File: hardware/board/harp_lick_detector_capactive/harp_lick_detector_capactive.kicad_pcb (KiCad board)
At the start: 4 copper layers, 80 x 50 mm, 170 parts, among them J2 Conn_01x03_Male, J3 Conn_Triaxial, J4 AudioJack3, J5 USB_C_Receptacle_USB2.0, J6 Barrel_Jack_Switch, J7 Conn_Coaxial, SW2 SW_DIP_x02, U1 74LVCH2T45DC, U11 LM27762, U12 LT3030, U13 ADS7049, U14 TS5A9411DCKR, U15 LTC6081xMS8, U16 AD8615, U17 AD8615, U18 TS5A9411DCKR, U2 TPD2EUSB30, U3 ADUM4160, U4 RP2040, U5 W25Q16JVUXIQ, U6 TS5A9411DCKR, U7 LTC6268xS8-10, U8 REF2025, U9 TS5A9411DCKR, X1 ECS-TXO-2016

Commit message: draft v0.8 pcb layout
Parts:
- removed C66: 100nF, Capacitor_SMD:C_0402_1005Metric
- removed U15: LTC6081xMS8, Package_SO:MSOP-8_3x3mm_P0.65mm
- removed U16: AD8615, Package_TO_SOT_SMD:TSOT-23-5
- added C68: 160pF, Capacitor_SMD:C_0402_1005Metric, F.Cu at (134.7, 87.2)
- added C69: 100nF, Capacitor_SMD:C_0402_1005Metric, F.Cu at (140.0, 99.9)
- added C70: 100nF, Capacitor_SMD:C_0402_1005Metric, F.Cu at (138.2, 95.2)
- added C71: 100nF, Capacitor_SMD:C_0402_1005Metric, F.Cu at (132.8, 82.0)
- added C72: 160pF, Capacitor_SMD:C_0402_1005Metric, F.Cu at (133.7, 87.2)
- added C73: 130pF, Capacitor_SMD:C_0402_1005Metric, F.Cu at (134.7, 98.8)
- added C74: 130pF, Capacitor_SMD:C_0402_1005Metric, F.Cu at (133.7, 98.8)
- added R60: 4K7, Resistor_SMD:R_0402_1005Metric, F.Cu at (145.0, 94.5)
- added R61: 4K7, Resistor_SMD:R_0402_1005Metric, F.Cu at (145.0, 95.5)
- added R62: 1K00, Resistor_SMD:R_0402_1005Metric, F.Cu at (141.0, 108.2)
- added R63: 1K00, Resistor_SMD:R_0402_1005Metric, F.Cu at (138.7, 106.5)
- added R64: 200K, Resistor_SMD:R_0402_1005Metric, F.Cu at (132.6, 85.9)
- added R65: 1K00, Resistor_SMD:R_0402_1005Metric, F.Cu at (136.4, 86.8)
- added R66: 100K, Resistor_SMD:R_0402_1005Metric, F.Cu at (134.2, 88.6)
- added R67: 9K76, Resistor_SMD:R_0402_1005Metric, F.Cu at (135.7, 88.2)
- added R68: 147, Resistor_SMD:R_0402_1005Metric, F.Cu at (135.8, 90.1)
- added R69: 249K, Resistor_SMD:R_0402_1005Metric, F.Cu at (132.6, 100.1)
- added R70: 976, Resistor_SMD:R_0402_1005Metric, F.Cu at (136.2, 99.4)
- added R71: 97K6, Resistor_SMD:R_0402_1005Metric, F.Cu at (134.2, 97.4)
- added R72: 8K66, Resistor_SMD:R_0402_1005Metric, F.Cu at (135.7, 97.9)
- added R73: 140, Resistor_SMD:R_0402_1005Metric, F.Cu at (135.8, 96.0)
- added U10: AD8652, Package_SO:MSOP-8_3x3mm_P0.65mm, F.Cu at (141.0, 104.5)
- R51, R53: value 100K -> 1K00
- U14, U18: value TS5A9411DCKR -> MAX4564EKA; footprint Package_TO_SOT_SMD:SOT-363_SC-70-6 -> Package_TO_SOT_SMD:SOT-23-8
- U6: value TS5A9411DCKR -> ADA4891-4; footprint Package_TO_SOT_SMD:SOT-363_SC-70-6 -> Package_SO:TSSOP-14_4.4x5mm_P0.65mm
- moved R52 14.7 mm to (141.0, 109.2), turned to 180 degrees
- moved U9 10.6 mm to (144.4, 104.5), turned to 180 degrees
- moved R49 10.5 mm to (138.3, 105.0), turned to 0 degrees
- moved C64 9.95 mm to (142.8, 109.0), turned to 90 degrees
- moved R51 9.79 mm to (138.3, 104.0), turned to 180 degrees
- moved C25 9.74 mm to (132.6, 88.2), turned to 90 degrees
- moved U6 9.12 mm to (132.6, 93.0)
- moved C60 8.57 mm to (145.4, 102.0), turned to 0 degrees
- moved C24 6.74 mm to (132.6, 97.8)
- moved R53 5.65 mm to (141.7, 99.8), turned to 0 degrees
- moved R46 5.17 mm to (129.3, 90.1), turned to 90 degrees
- moved R56 5.14 mm to (128.0, 82.4)
- moved R24 4.54 mm to (127.8, 98.2), turned to 0 degrees
- moved R27 3.83 mm to (129.4, 88.2), turned to 90 degrees
- moved R19 3.69 mm to (127.9, 86.8), turned to 0 degrees
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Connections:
- C1 pad 2: +3V3 -> +3.3V
- C10 pad 1: +3V3 -> +3.3V
- C11 pad 1: +3V3 -> +3.3V
- C12 pad 2: +3V3 -> +3.3V
- C13 pad 2: +3V3 -> +3.3V
- C14 pad 2: +3V3 -> +3.3V
- C15 pad 2: +3V3 -> +3.3V
- C16 pad 2: +3V3 -> +3.3V
- C17 pad 2: +3V3 -> +3.3V
- C18 pad 2: +3V3 -> +3.3V
- C19 pad 2: +3V3 -> +3.3V
- C29 pad 1: GND -> +2V5
- C29 pad 2: +3V3 -> GND
- C3 pad 2: +3V3 -> +3.3V
- C31 pad 2: Net-(U15B--) -> Net-(U6D--)
- C34 pad 2: Net-(U15A--) -> Net-(U6A--)
- C4 pad 2: +3V3 -> +3.3V
- C47 pad 1: +3V3 -> +3.3V
- C48 pad 1: +3V3 -> +3.3V
- C5 pad 2: +3V3 -> +3.3V
- C51 pad 2: +3V3 -> +3.3V
- C53 pad 1: +3V3 -> +3.3V
- C54 pad 2: +3V3 -> +3.3V
- C60 pad 2: +3V3 -> +3.3V
- C63 pad 2: +3V3 -> +2V5
- C64 pad 2: +3V3 -> +2V5
- C65 pad 2: +2V5 -> VREF_1V25
- C8 pad 1: +3V3 -> +3.3V
- D4 pad 2: +3V3 -> +3.3V
- J4 pad R: +3V3 -> +3.3V
- R20 pad 1: Net-(U15B--) -> Net-(U6D--)
- R21 pad 2: Net-(U16-+) -> Net-(U10A-+)
- R22 pad 1: Net-(U16--) -> Net-(U10A--)
- R23 pad 1: Net-(U7--) -> Net-(C33-Pad1)
- R23 pad 2: Net-(C33-Pad1) -> Net-(U7--)
- R26 pad 1: Net-(U15A--) -> Net-(U6A--)
- R27 pad 1: Net-(U15B-+) -> Net-(U6D-+)
- R39 pad 1: +3V3 -> +3.3V
- R43 pad 2: Net-(R22-Pad2) -> Net-(R43-Pad2)
- R46 pad 2: Net-(U15B-+) -> Net-(U6D-+)
- R47 pad 2: Net-(U15A-+) -> Net-(U6A-+)
- R48 pad 1: Net-(U15A-+) -> Net-(U6A-+)
- R49 pad 2: Net-(R49-Pad2) -> Net-(U10B-+)
- R51 pad 1: Net-(R51-Pad1) -> Net-(U10A-+)
- R51 pad 2: Net-(R49-Pad2) -> Net-(R49-Pad1)
- R52 pad 1: Net-(R52-Pad1) -> GND
- R52 pad 2: GND -> Net-(U10B--)
- R53 pad 1: Net-(R53-Pad1) -> Net-(U10A--)
- R57 pad 2: +3V3 -> +3.3V
- R58 pad 2: +3V3 -> +3.3V
- R9 pad 2: +3V3 -> +3.3V
- TP1 pad 1: Net-(R22-Pad2) -> Net-(R43-Pad2)
- U1 pad 1: +3V3 -> +3.3V
- U1 pad 5: +3V3 -> +3.3V
- U12 pad 7: +3V3 -> +3.3V
- U12 pad 8: +3V3 -> +3.3V
- U13 pad 1: +3V3 -> +3.3V
- U14 pad 1: FILTER_SEL -> Net-(C68-Pad2)
- U14 pad 2: +3V3 -> +2V5
- U14 pad 3: GND -> FREQ_SEL
- U14 pad 4: Net-(C30-Pad2) -> Net-(C73-Pad2)
- U14 pad 5: Net-(R49-Pad2) -> GND
- U14 pad 6: Net-(C33-Pad2) -> -2V5
- U18 pad 1: GAIN_SEL -> Net-(R56-Pad1)
- U18 pad 2: +3V3 -> +2V5
- U18 pad 3: GND -> GAIN_SEL
- U18 pad 4: Net-(R56-Pad1) -> Net-(R54-Pad1)
- U18 pad 5: Net-(U17--) -> GND
- U18 pad 6: Net-(R54-Pad1) -> -2V5
- U3 pad 12: +3V3 -> +3.3V
- U3 pad 13: +3V3 -> +3.3V
- U3 pad 14: +3V3 -> +3.3V
- U3 pad 16: +3V3 -> +3.3V
- U4 pad 1: +3V3 -> +3.3V
- U4 pad 10: +3V3 -> +3.3V
- U4 pad 22: +3V3 -> +3.3V
- U4 pad 26: +3V3 -> +3.3V
- U4 pad 27: FILTER_SEL -> Net-(U4-GPIO16)
- U4 pad 28: GAIN_SEL -> Net-(U4-GPIO17)
- U4 pad 33: +3V3 -> +3.3V
- U4 pad 42: +3V3 -> +3.3V
- U4 pad 43: +3V3 -> +3.3V
- U4 pad 44: +3V3 -> +3.3V
- U4 pad 48: +3V3 -> +3.3V
- U4 pad 49: +3V3 -> +3.3V
- U5 pad 8: +3V3 -> +3.3V
- U6 pad 1: GAIN_SEL -> Net-(C33-Pad2)
- U6 pad 2: +3V3 -> Net-(U6A--)
- U6 pad 3: GND -> Net-(U6A-+)
- U6 pad 4: Net-(R52-Pad1) -> +2V5
- U6 pad 5: Net-(U16--) -> Net-(U6B-+)
- U6 pad 6: Net-(R53-Pad1) -> Net-(U6B--)
- U9 pad 2: +3V3 -> +3.3V
- U9 pad 4: Net-(R49-Pad1) -> Net-(R22-Pad2)
- U9 pad 5: Net-(U16-+) -> Net-(R43-Pad2)
- U9 pad 6: Net-(R51-Pad1) -> Net-(R62-Pad2)
- X1 pad 4: +3V3 -> +3.3V
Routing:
- net +3V3: track 106.2 -> 0.00 mm, vias 33 -> 0
- net +3.3V: track 0.00 -> 93.2 mm, vias 0 -> 29
- net GAIN_SEL: track 47.8 -> 10.3 mm, vias 5 -> 0
- net -2V5: track 29.8 -> 47.4 mm, vias 6 -> 10
- net Net-(R43-Pad2): track 0.00 -> 17.3 mm, vias 0 -> 1
- net Net-(R22-Pad2): track 20.4 -> 4.15 mm
- net Net-(U16--): track 15.1 -> 0.00 mm
- net Net-(R49-Pad1): track 1.26 -> 14.7 mm
- net +2V5: track 16.3 -> 28.0 mm, vias 6 -> 9
- net FILTER_SEL: track 10.2 -> 0.00 mm
- net Net-(U16-+): track 9.99 -> 0.00 mm, vias 2 -> 0
- net Net-(C73-Pad2): track 0.00 -> 8.64 mm
- net Net-(C68-Pad2): track 0.00 -> 8.39 mm
- net Net-(U6D-+): track 0.00 -> 5.75 mm
- net Net-(U6C-+): track 0.00 -> 5.63 mm
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- added copper zone on F.Cu, net +3.3V
- added copper zone on In2.Cu, net +3.3V
- removed copper zone on F.Cu, net +3V3
- removed copper zone on In2.Cu, net +3V3
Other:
- board text added: "Ground Lug"
- board text added: "v0.8.0, May 6, 2024"
- board text removed: "Chassis Ground"
- board text removed: "v0.7.0, April 9, 2024"

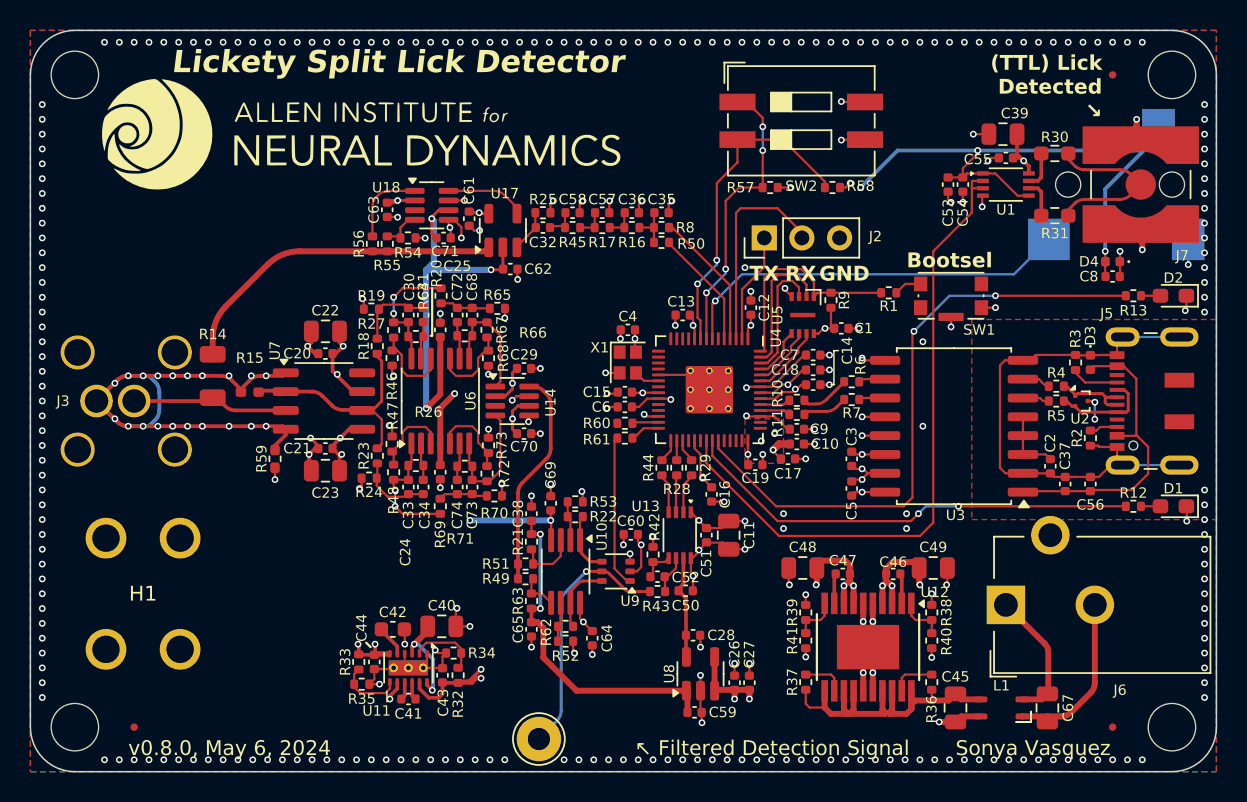
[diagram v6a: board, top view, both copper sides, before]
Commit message: update board with filter resistor values
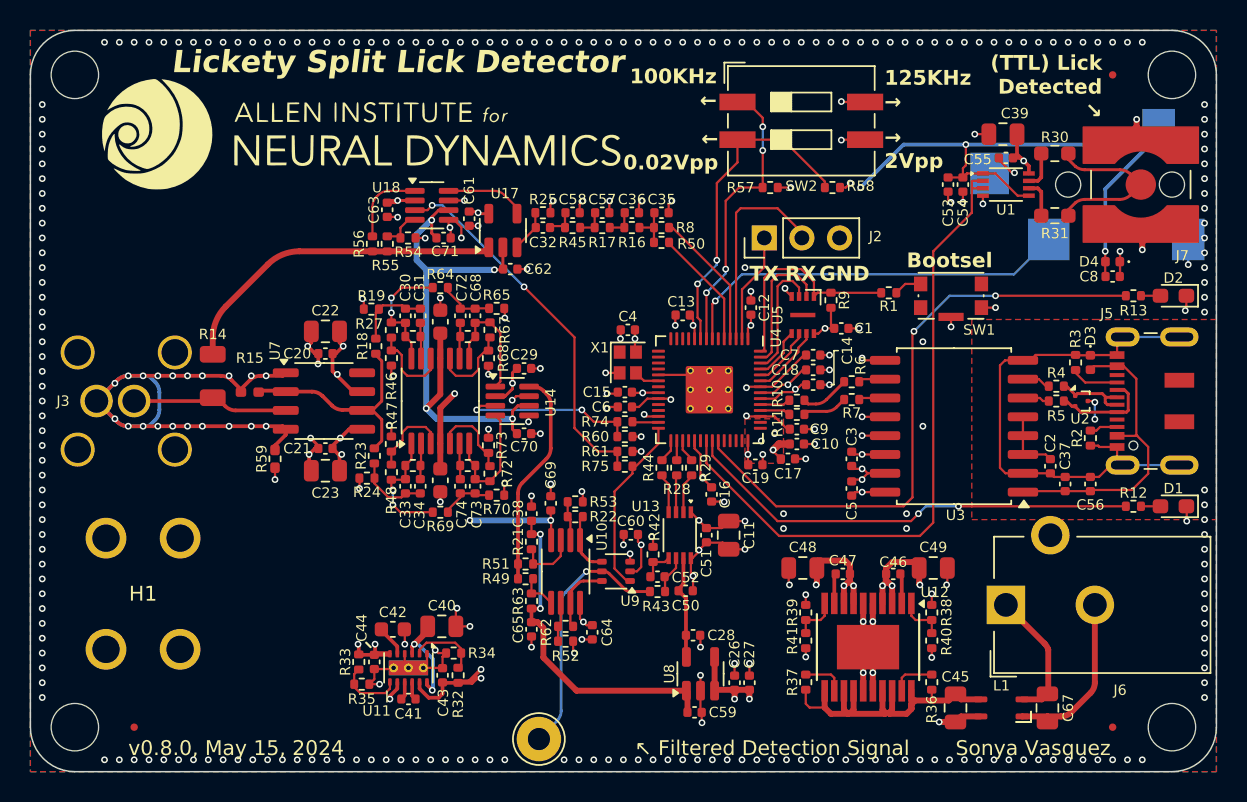
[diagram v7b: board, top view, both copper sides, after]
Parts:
- added R74: 1K00, Resistor_SMD:R_0402_1005Metric, F.Cu at (145.0, 94.4)
- added R75: 1K00, Resistor_SMD:R_0402_1005Metric, F.Cu at (145.0, 97.4)
- C24, C25: footprint Capacitor_SMD:C_0402_1005Metric -> Capacitor_SMD:C_0603_1608Metric
- J4: footprint Connector_Audio:Jack_3.5mm_CUI_SJ-3523-SMT_Horizontal -> Connector_Audio:Jack_3.5mm_CUI_SJ-3524-SMT_Horizontal
- moved R60 0.90 mm to (145.0, 95.4), turned to 0 degrees
- moved R61 0.90 mm to (145.0, 96.4), turned to 0 degrees
- moved R64 0.55 mm to (132.6, 85.3), turned to 180 degrees
- moved C24 0.55 mm to (132.6, 98.3)
- moved C25 0.55 mm to (132.6, 87.7)
- moved C64 0.40 mm to (142.8, 108.6)
- moved R69 0.40 mm to (132.6, 100.5), turned to 180 degrees
- moved R66 0.21 mm to (134.4, 88.7)
- moved R71 0.21 mm to (134.4, 97.3)
- moved C30 0.21 mm to (130.2, 87.2)
- moved C31 0.21 mm to (131.2, 87.2)
- moved C33 0.21 mm to (130.2, 98.8)
- moved C34 0.21 mm to (131.2, 98.8)
- moved C68 0.21 mm to (134.9, 87.2)
- moved C72 0.21 mm to (133.9, 87.2)
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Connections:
- R60 pad 1: Net-(U4-GPIO16) -> FREQ_SEL_2V5
- R60 pad 2: FREQ_SEL -> GND
- R61 pad 1: Net-(U4-GPIO17) -> GAIN_SEL_2V5
- R61 pad 2: GAIN_SEL -> GND
- U14 pad 3: FREQ_SEL -> FREQ_SEL_2V5
- U18 pad 3: GAIN_SEL -> GAIN_SEL_2V5
- U4 pad 27: Net-(U4-GPIO16) -> FREQ_SEL
- U4 pad 28: Net-(U4-GPIO17) -> GAIN_SEL
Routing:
- net GAIN_SEL_2V5: track 0.00 -> 25.3 mm, vias 0 -> 2
- net FREQ_SEL_2V5: track 0.00 -> 12.2 mm, vias 0 -> 2
- net -2V5: track 47.4 -> 54.2 mm
- net GND: track 118.4 -> 120.9 mm, vias 310 -> 313
- net Net-(U4-GPIO17): track 2.03 -> 0.00 mm
- net GAIN_SEL: track 10.3 -> 12.2 mm
- net Net-(U4-GPIO16): track 1.78 -> 0.00 mm
- net FREQ_SEL: track 0.00 -> 1.77 mm
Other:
- board text added: "v0.8.0, May 15, 2024"
- board text removed: "v0.8.0, May 6, 2024"
